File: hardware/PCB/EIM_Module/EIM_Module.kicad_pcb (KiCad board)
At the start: 4 copper layers, 164 parts, among them J1 ADC, J2 CURRENT_PUMP_2, J3 VOLTAGE_MEASUREMENT_1, J4 VOLTAGE_MEASUREMENT_2, J5 PROG, J7 Digital PSU, J8 CURRENT_PUMP_1, J9 Analog PSU, U1 AD9834BRUZ, U10 AD8066ARZ-R7, U2 AD8130ARZ, U3 AD8014ARZ, U4 AD8130ARZ, U5 AD8066ARZ-R7, U6 AD8130ARZ, U7 AD8066ARZ-R7, U8 AD8130ARZ, U9 AD8302ARUZ, Y2 75MHz

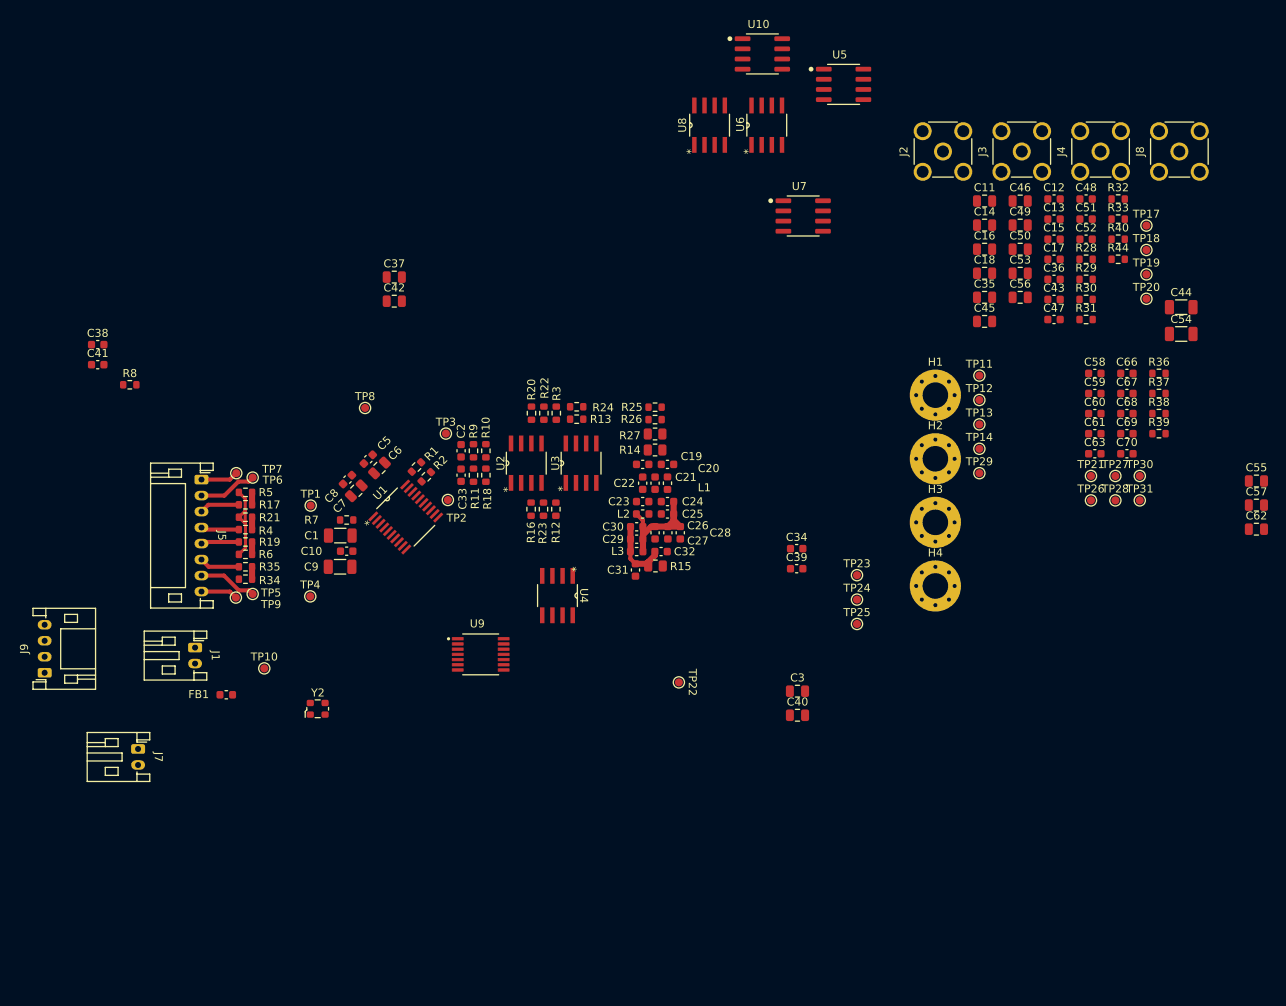
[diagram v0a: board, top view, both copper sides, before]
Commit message: MAMS-38 updated PCB layout for EIM with version using connector
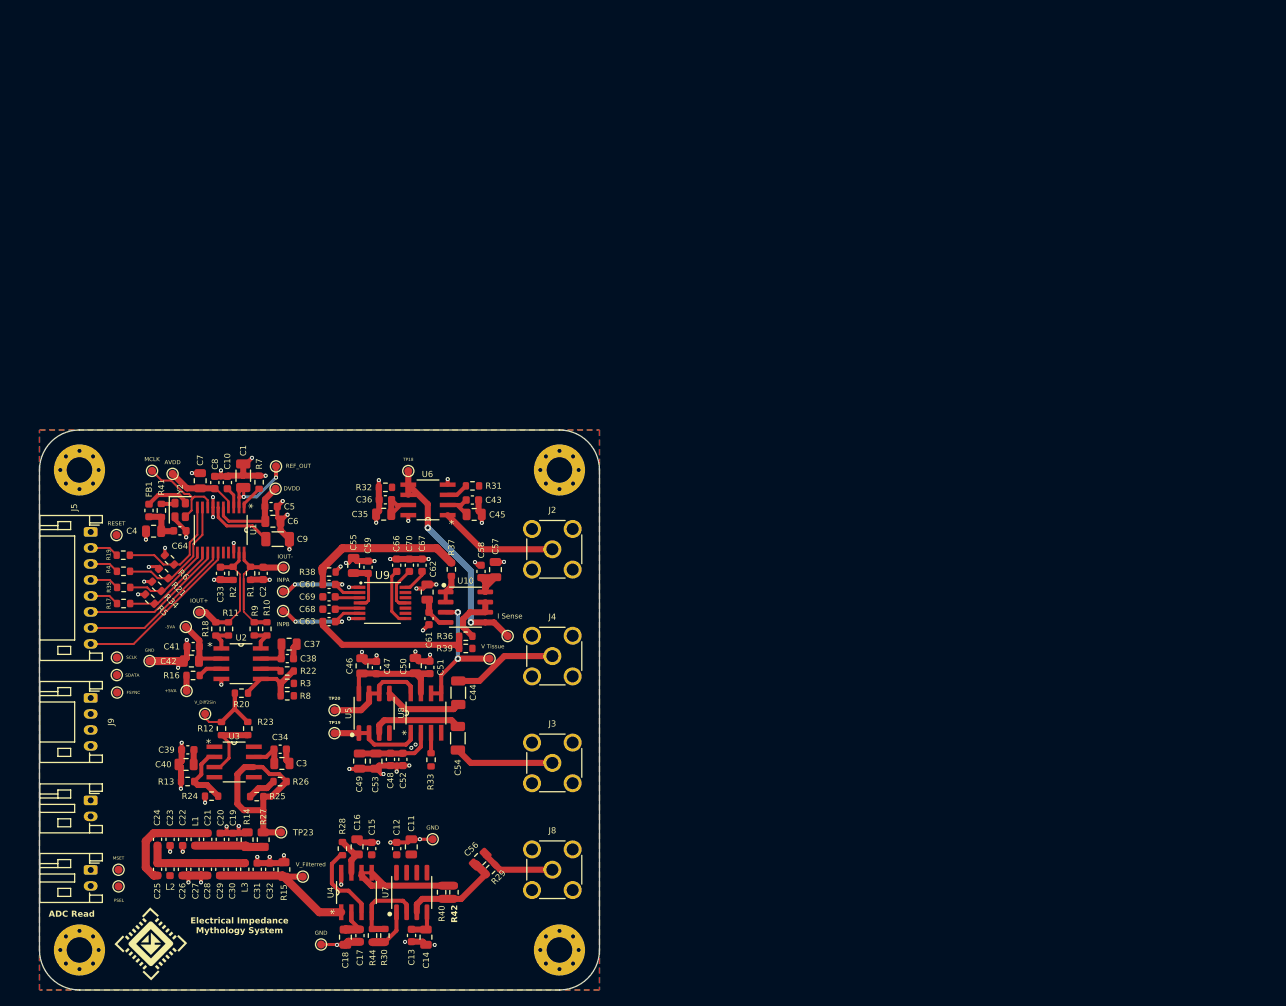
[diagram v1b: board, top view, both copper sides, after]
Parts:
- removed TP1: TP_REFOUT, TestPoint:TestPoint_Pad_D1.0mm
- removed TP10: TP_DIF_SIN, TestPoint:TestPoint_Pad_D1.0mm
- removed TP11: 3.3D, TestPoint:TestPoint_Pad_D1.0mm
- removed TP12: 5VA, TestPoint:TestPoint_Pad_D1.0mm
- removed TP13: -5VA, TestPoint:TestPoint_Pad_D1.0mm
- removed TP14, TP25: GND, TestPoint:TestPoint_Pad_D1.0mm
- removed TP17, TP26: VOUT_BUFFER, TestPoint:TestPoint_Pad_D1.0mm
- removed TP2: TP_IOUT, TestPoint:TestPoint_Pad_D1.0mm
- removed TP21, TP22: VOUT_FILTERED, TestPoint:TestPoint_Pad_D1.0mm
- removed TP24, TP27: VIN_DiffToSingle, TestPoint:TestPoint_Pad_D1.0mm
- removed TP28, TP30, TP31, TP9: TP_GND, TestPoint:TestPoint_Pad_D1.0mm
- removed TP29: 3.3AV, TestPoint:TestPoint_Pad_D1.0mm
- removed TP3: TP_IOUTB, TestPoint:TestPoint_Pad_D1.0mm
- removed TP4: TP_RESET, TestPoint:TestPoint_Pad_D1.0mm
- removed TP5: TP_SDATA, TestPoint:TestPoint_Pad_D1.0mm
- removed TP6: TP_SCLK, TestPoint:TestPoint_Pad_D1.0mm
- removed TP7: TP_FSYNC, TestPoint:TestPoint_Pad_D1.0mm
- removed TP8: TP_MCLK, TestPoint:TestPoint_Pad_D1.0mm
- added +5VA: 5VA, TestPoint:TestPoint_Pad_D1.0mm, F.Cu at (118.4, 102.6)
- added -5VA: -5VA, TestPoint:TestPoint_Pad_D1.0mm, F.Cu at (118.3, 94.6)
- added AVDD: 3.3AV, TestPoint:TestPoint_Pad_D1.0mm, F.Cu at (116.6, 75.5)
- added C4: 10u, Capacitor_SMD:C_0805_2012Metric, F.Cu at (114.3, 82.7)
- added C64: 0.1u, Capacitor_SMD:C_0603_1608Metric, F.Cu at (117.6, 82.6)
- added DVDD: 3.3D, TestPoint:TestPoint_Pad_D1.0mm, F.Cu at (129.5, 77.3)
- added FSYNC: TP_FSYNC, TestPoint:TestPoint_Pad_D1.0mm, F.Cu at (109.7, 102.8)
- added G***: LOGO, dpee_logo_kicad:dpee-logo_10x10, F.Cu at (114.0, 134.2)
- added G***: LOGO, dpee_logo_kicad:DPEE_Footprint, B.Cu at (124.6, 100.7)
- added GND: GND, TestPoint:TestPoint_Pad_D1.0mm, F.Cu at (149.1, 121.2)
- added GND: GND, TestPoint:TestPoint_Pad_D1.0mm, F.Cu at (113.8, 98.9)
- added GND: TP_GND, TestPoint:TestPoint_Pad_D1.0mm, F.Cu at (135.2, 134.3)
- added I Sense: VIN_DiffToSingle, TestPoint:TestPoint_Pad_D1.0mm, F.Cu at (158.5, 95.8)
- added INPA: VOUT_FILTERED, TestPoint:TestPoint_Pad_D1.0mm, F.Cu at (130.5, 90.2)
- added INPB: TP_GND, TestPoint:TestPoint_Pad_D1.0mm, F.Cu at (130.5, 92.6)
- added IOUT+: TP_IOUT, TestPoint:TestPoint_Pad_D1.0mm, F.Cu at (120.0, 92.8)
- added IOUT-: TP_IOUTB, TestPoint:TestPoint_Pad_D1.0mm, F.Cu at (130.5, 87.2)
- added MCLK: TP_MCLK, TestPoint:TestPoint_Pad_D1.0mm, F.Cu at (114.1, 75.1)
- added MSET: TP_GND, TestPoint:TestPoint_Pad_D1.0mm, F.Cu at (109.9, 125.0)
- added PSEL: TP_GND, TestPoint:TestPoint_Pad_D1.0mm, F.Cu at (109.9, 127.1)
- added R41: 10K, Resistor_SMD:R_0603_1608Metric, F.Cu at (115.2, 80.1)
- added R42: 10k, Resistor_SMD:R_0603_1608Metric, F.Cu at (151.8, 127.8)
- added REF_OUT: TP_REFOUT, TestPoint:TestPoint_Pad_D1.0mm, F.Cu at (129.6, 74.5)
- added RESET: TP_RESET, TestPoint:TestPoint_Pad_D1.0mm, F.Cu at (109.6, 83.1)
- added SCLK: TP_SCLK, TestPoint:TestPoint_Pad_D1.0mm, F.Cu at (109.7, 98.5)
- added SDATA: TP_SDATA, TestPoint:TestPoint_Pad_D1.0mm, F.Cu at (109.7, 100.6)
- added V Tissue: VOUT_BUFFER, TestPoint:TestPoint_Pad_D1.0mm, F.Cu at (156.3, 98.6)
- added V_Diff2Sin: TP_DIF_SIN, TestPoint:TestPoint_Pad_D1.0mm, F.Cu at (120.7, 105.5)
- added V_Filterred: VOUT_FILTERED, TestPoint:TestPoint_Pad_D1.0mm, F.Cu at (132.9, 125.8)
- Y2: footprint Oscillator:Oscillator_SMD_ECS_2520MV-xxx-xx-4Pin_2.5x2.0mm -> Oscillator:Oscillator_SMD_SeikoEpson_SG210-4Pin_2.5x2.0mm
- moved R44 125.8 mm to (141.6, 133.2), turned to -90 degrees
- moved C17 121.1 mm to (140.1, 133.2), turned to 90 degrees
- moved C13 120.3 mm to (146.5, 133.2), turned to 90 degrees
- moved H3 119.6 mm to (105.0, 135.0)
- moved J8 119.2 mm to (164.1, 125.0), turned to -90 degrees
- moved R28 118.6 mm to (137.9, 122.3), turned to -90 degrees
- moved R30 118.3 mm to (143.2, 133.2), turned to -90 degrees
- moved R40 117.5 mm to (150.3, 127.8), turned to -90 degrees
- moved TP19 116.6 mm to (136.9, 107.9)
- moved C12 115.5 mm to (144.7, 122.3), turned to -90 degrees
- moved C18 115.2 mm to (138.2, 133.4), turned to 90 degrees
- moved C15 114.4 mm to (141.5, 122.3), turned to -90 degrees
- moved TP20 113.8 mm to (136.9, 105.0)
- moved C55 113.3 mm to (139.3, 86.9), turned to -90 degrees
- moved C14 113.1 mm to (148.3, 133.4), turned to 90 degrees
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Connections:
- net /Voltage Controlled Current Source & Load/+IN_LOAD renamed /Voltage Controlled Current Source & Load/IN_LOAD+
- net /Voltage Controlled Current Source & Load/-IN_LOAD renamed /Voltage Controlled Current Source & Load/IN_LOAD-
- C1 pad 2: AGND -> GND
- C10 pad 1: AGND -> GND
- C11 pad 1: AGND -> GND
- C12 pad 1: AGND -> GND
- C13 pad 1: AGND -> GND
- C14 pad 1: AGND -> GND
- C15 pad 1: AGND -> GND
- C16 pad 1: AGND -> GND
- C17 pad 1: AGND -> GND
- C18 pad 1: AGND -> GND
- C19 pad 1: AGND -> GND
- C2 pad 1: AGND -> GND
- C20 pad 1: AGND -> GND
- C22 pad 1: AGND -> GND
- C23 pad 1: AGND -> GND
- C26 pad 1: AGND -> GND
- C27 pad 1: AGND -> GND
- C28 pad 1: AGND -> GND
- C3 pad 1: AGND -> GND
- C31 pad 1: AGND -> GND
- C32 pad 1: AGND -> GND
- C33 pad 1: AGND -> GND
- C34 pad 1: AGND -> GND
- C35 pad 1: AGND -> GND
- C36 pad 1: AGND -> GND
- C37 pad 1: AGND -> GND
- C38 pad 1: AGND -> GND
- C39 pad 1: AGND -> GND
- C40 pad 1: AGND -> GND
- C41 pad 1: AGND -> GND
- C42 pad 1: AGND -> GND
- C43 pad 1: AGND -> GND
- C45 pad 1: AGND -> GND
- C46 pad 1: AGND -> GND
- C47 pad 1: AGND -> GND
- C48 pad 1: AGND -> GND
- C49 pad 1: AGND -> GND
- C5 pad 1: AGND -> GND
- C50 pad 1: AGND -> GND
- C51 pad 1: AGND -> GND
- C52 pad 1: AGND -> GND
- C53 pad 1: AGND -> GND
- C55 pad 1: AGND -> GND
- C57 pad 1: AGND -> GND
- C58 pad 1: AGND -> GND
- C59 pad 1: AGND -> GND
- C6 pad 1: AGND -> GND
- C61 pad 1: AGND -> GND
- C62 pad 1: AGND -> GND
- C66 pad 2: AGND -> GND
- C67 pad 2: AGND -> GND
- C68 pad 1: AGND -> GND
- C69 pad 1: AGND -> GND
- C7 pad 1: AGND -> GND
- C70 pad 1: AGND -> GND
- C8 pad 1: AGND -> GND
- C9 pad 1: AGND -> GND
- H1 pad 1: AGND -> GND
- H2 pad 1: AGND -> GND
- H3 pad 1: AGND -> GND
- H4 pad 1: AGND -> GND
- J2 pad 2: AGND -> GND
- J3 pad 2: AGND -> GND
- J4 pad 2: AGND -> GND
- J5 pad 1: /Signal Generator & Differential to Single/FSYNC -> GND
- J5 pad 2: /Signal Generator & Differential to Single/SCLK -> /Signal Generator & Differential to Single/PSELECT_uC
- J5 pad 3: /Signal Generator & Differential to Single/PIN_3 -> /Signal Generator & Differential to Single/FSELECT_uC
- J5 pad 4: Net-(J5-Pin_4) -> /Signal Generator & Differential to Single/RESET_uC
- J5 pad 5: /Signal Generator & Differential to Single/PIN_5 -> /Signal Generator & Differential to Single/SLEEP_uC
- J5 pad 6: /Signal Generator & Differential to Single/PIN_6 -> /Signal Generator & Differential to Single/SDATA
- J5 pad 7: /Signal Generator & Differential to Single/SDATA -> /Signal Generator & Differential to Single/SCLK
- J5 pad 8: AGND -> /Signal Generator & Differential to Single/FSYNC
- J7 pad 1: AGND -> GND
- J8 pad 2: AGND -> GND
- J9 pad 1: AGND -> GND
- R1 pad 1: AGND -> GND
- R13 pad 1: AGND -> GND
- R14 pad 1: AGND -> GND
- R15 pad 1: AGND -> GND
- R17 pad 1: /Signal Generator & Differential to Single/PIN_3 -> /Signal Generator & Differential to Single/SLEEP_uC
- R19 pad 1: /Signal Generator & Differential to Single/PIN_5 -> /Signal Generator & Differential to Single/PSELECT_uC
- R2 pad 1: AGND -> GND
- R21 pad 1: AGND -> GND
- R24 pad 1: AGND -> GND
- R3 pad 1: AGND -> GND
- R32 pad 2: AGND -> GND
- R34 pad 1: AGND -> GND
- R35 pad 1: /Signal Generator & Differential to Single/PIN_6 -> /Signal Generator & Differential to Single/RESET_uC
- R38 pad 1: AGND -> GND
- R39 pad 1: AGND -> GND
- R4 pad 1: Net-(J5-Pin_4) -> /Signal Generator & Differential to Single/FSELECT_uC
- R5 pad 1: AGND -> GND
- R6 pad 1: AGND -> GND
- R7 pad 1: AGND -> GND
- R8 pad 1: AGND -> GND
- U1 pad 18: AGND -> GND
- U1 pad 7: AGND -> GND
- U2 pad 4: AGND -> GND
- U4 pad 8: AGND -> GND
- U6 pad 4: AGND -> GND
- U6 pad 8: AGND -> GND
- U7 pad 5: AGND -> GND
- U8 pad 4: AGND -> GND
- U9 pad 1: AGND -> GND
- U9 pad 7: AGND -> GND
- Y2 pad 1: unconnected-(Y2-Tri-State-Pad1) -> Net-(Y2-Tri-State)
- Y2 pad 2: AGND -> GND
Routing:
- net GND: track 0.00 -> 135.7 mm, vias 0 -> 67
- net +5V: track 0.00 -> 51.3 mm
- net -5V: track 0.00 -> 37.7 mm
- net /Gain & Phase detector/I_SENSE_RAW: track 0.00 -> 28.7 mm, vias 0 -> 2
- net /Buffer & Filter blocks/VOUT_BUFFER: track 0.00 -> 25.0 mm
- net /Gain & Phase detector/to_INPB: track 0.00 -> 20.2 mm
- net /Gain & Phase detector/to_INPA: track 0.00 -> 20.0 mm
- net /Signal Generator & Differential to Single/IOUT+: track 0.00 -> 19.7 mm
- net /Signal Generator & Differential to Single/IOUT-: track 0.00 -> 19.6 mm
- net /Gain & Phase detector/V_TISSUE_RAW: track 0.00 -> 17.8 mm, vias 0 -> 2
- net /Voltage Controlled Current Source & Load/FB_VCCS: track 0.00 -> 17.5 mm
- net /Signal Generator & Differential to Single/FSYNC: track 4.68 -> 21.2 mm
- net +3.3V: track 0.00 -> 16.1 mm
- net AGND: track 15.3 -> 0.00 mm
- net /Voltage Controlled Current Source & Load/CURRENT_PUMP_2: track 0.00 -> 14.8 mm
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- added copper zone on B.Cu, net GND
- added copper zone on F.Cu, net GND
- added copper zone on In1.Cu, net GND
- added copper zone on In2.Cu, net GND
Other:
- board outline added: 70 x 70 mm
- board text added: "ADC Read"
- board text added: "Electrical Impedance Mythology System"

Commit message: MAMS-40 Updated PCB upto LPF
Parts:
- removed +5VA: 5VA, TestPoint:TestPoint_Pad_D1.0mm
- removed -5VA: -5VA, TestPoint:TestPoint_Pad_D1.0mm
- removed AVDD: 3.3AV, TestPoint:TestPoint_Pad_D1.0mm
- removed C70: 0.1u, Capacitor_SMD:C_0603_1608Metric
- removed DVDD: 3.3D, TestPoint:TestPoint_Pad_D1.0mm
- removed FSYNC: TP_FSYNC, TestPoint:TestPoint_Pad_D1.0mm
- removed the G*** at (114.0, 134.2)
- removed GND (x2): GND, TestPoint:TestPoint_Pad_D1.0mm
- removed GND, INPB, MSET, PSEL: TP_GND, TestPoint:TestPoint_Pad_D1.0mm
- removed I Sense: VIN_DiffToSingle, TestPoint:TestPoint_Pad_D1.0mm
- removed INPA, V_Filterred: VOUT_FILTERED, TestPoint:TestPoint_Pad_D1.0mm
- removed IOUT+: TP_IOUT, TestPoint:TestPoint_Pad_D1.0mm
- removed IOUT-: TP_IOUTB, TestPoint:TestPoint_Pad_D1.0mm
- removed J1: ADC, Connector_JST:JST_PH_S2B-PH-K_1x02_P2.00mm_Horizontal
- removed J7: Digital PSU, Connector_JST:JST_PH_S2B-PH-K_1x02_P2.00mm_Horizontal
- removed J9: Analog PSU, Connector_JST:JST_PH_S4B-PH-K_1x04_P2.00mm_Horizontal
- removed MCLK: TP_MCLK, TestPoint:TestPoint_Pad_D1.0mm
- removed REF_OUT: TP_REFOUT, TestPoint:TestPoint_Pad_D1.0mm
- removed RESET: TP_RESET, TestPoint:TestPoint_Pad_D1.0mm
- removed SCLK: TP_SCLK, TestPoint:TestPoint_Pad_D1.0mm
- removed SDATA: TP_SDATA, TestPoint:TestPoint_Pad_D1.0mm
- removed V Tissue: VOUT_BUFFER, TestPoint:TestPoint_Pad_D1.0mm
- removed V_Diff2Sin: TP_DIF_SIN, TestPoint:TestPoint_Pad_D1.0mm
- added G***: LOGO, dpee_logo_kicad:dpee-logo_6x6, F.Cu at (144.0, 87.5)
- added TP1: TP_REFOUT, TestPoint:TestPoint_Pad_D1.0mm, F.Cu at (358.2, -9.72)
- added TP10: TP_DIF_SIN, TestPoint:TestPoint_Pad_D1.0mm, F.Cu at (361.2, 2.48)
- added TP11: 3.3D, TestPoint:TestPoint_Pad_D1.0mm, F.Cu at (368.5, 34.8)
- added TP12: 5VA, TestPoint:TestPoint_Pad_D1.0mm, F.Cu at (368.5, 37.9)
- added TP13: -5VA, TestPoint:TestPoint_Pad_D1.0mm, F.Cu at (368.5, 40.9)
- added TP14: GND, TestPoint:TestPoint_Pad_D1.0mm, F.Cu at (368.5, 44.0)
- added TP17: VOUT_BUFFER, TestPoint:TestPoint_Pad_D1.0mm, F.Cu at (353.1, 12.5)
- added TP2: TP_IOUT, TestPoint:TestPoint_Pad_D1.0mm, F.Cu at (358.2, -6.67)
- added TP21: VOUT_FILTERED, TestPoint:TestPoint_Pad_D1.0mm, F.Cu at (338.3, 34.8)
- added TP22: VOUT_FILTERED, TestPoint:TestPoint_Pad_D1.0mm, F.Cu at (331.8, 34.8)
- added TP25: GND, TestPoint:TestPoint_Pad_D1.0mm, F.Cu at (331.8, 40.9)
- added TP27: VIN_DiffToSingle, TestPoint:TestPoint_Pad_D1.0mm, F.Cu at (338.3, 37.9)
- added TP28: TP_GND, TestPoint:TestPoint_Pad_D1.0mm, F.Cu at (338.3, 40.9)
- added TP29: 3.3AV, TestPoint:TestPoint_Pad_D1.0mm, F.Cu at (368.5, 47.0)
- added TP3: TP_IOUTB, TestPoint:TestPoint_Pad_D1.0mm, F.Cu at (358.2, -3.62)
- added TP30: TP_GND, TestPoint:TestPoint_Pad_D1.0mm, F.Cu at (338.3, 44.0)
- added TP31: TP_GND, TestPoint:TestPoint_Pad_D1.0mm, F.Cu at (338.3, 47.0)
- added TP4: TP_RESET, TestPoint:TestPoint_Pad_D1.0mm, F.Cu at (358.2, -0.57)
- added TP5: TP_SDATA, TestPoint:TestPoint_Pad_D1.0mm, F.Cu at (358.2, 2.48)
- added TP6: TP_SCLK, TestPoint:TestPoint_Pad_D1.0mm, F.Cu at (361.2, -9.72)
- added TP7: TP_FSYNC, TestPoint:TestPoint_Pad_D1.0mm, F.Cu at (361.2, -6.67)
- added TP8: TP_MCLK, TestPoint:TestPoint_Pad_D1.0mm, F.Cu at (361.2, -3.62)
- added TP9: TP_GND, TestPoint:TestPoint_Pad_D1.0mm, F.Cu at (361.2, -0.57)
- C3: value 10u -> 20p; footprint Capacitor_SMD:C_0805_2012Metric -> Capacitor_SMD:C_0603_1608Metric
- C33: value 20p -> 10u; footprint Capacitor_SMD:C_0603_1608Metric -> Capacitor_SMD:C_0805_2012Metric
- J5: value PROG -> Interface with controller; footprint Connector_JST:JST_PH_S8B-PH-K_1x08_P2.00mm_Horizontal -> Connector_PinHeader_2.00mm:PinHeader_2x14_P2.00mm_Vertical; moved to B.Cu
- moved TP19 233.9 mm to (353.1, 18.6)
- moved TP20 231.7 mm to (353.1, 21.6)
- moved TP23 217.8 mm to (331.8, 37.9)
- moved TP18 215.4 mm to (353.1, 15.5)
- moved H3 98.5 mm to (145.0, 45.0)
- moved H1 94.9 mm to (195.0, 45.0)
- moved C3 61.5 mm to (159.4, 57.5), turned to 90 degrees
- moved C4 60.7 mm to (165.6, 50.4), turned to 180 degrees
- moved C68 59.7 mm to (184.5, 57.4)
- moved C49 59.2 mm to (184.6, 72.4), turned to 0 degrees
- moved C64 58.7 mm to (165.4, 48.6)
- moved C69 57.4 mm to (184.5, 59.9)
- moved C55 57.2 mm to (184.5, 51.8), turned to 0 degrees
- moved C35 56.3 mm to (185.0, 43.0)
- moved R38 54.5 mm to (184.5, 62.4), turned to 0 degrees
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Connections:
- C11 pad 2: +5V -> +5VA
- C12 pad 2: +5V -> +5VA
- C13 pad 2: -5V -> -5VA
- C14 pad 2: -5V -> -5VA
- C15 pad 2: +5V -> +5VA
- C16 pad 2: +5V -> +5VA
- C17 pad 2: -5V -> -5VA
- C18 pad 2: -5V -> -5VA
- C3 pad 2: +5V -> /Signal Generator & Differential to Single/IOUT+
- C33 pad 2: /Signal Generator & Differential to Single/IOUT+ -> +5VA
- C34 pad 2: +5V -> +5VA
- C35 pad 2: +5V -> +5VA
- C36 pad 2: +5V -> +5VA
- C37 pad 2: +5V -> +5VA
- C38 pad 2: +5V -> +5VA
- C39 pad 2: -5V -> -5VA
- C40 pad 2: -5V -> -5VA
- C41 pad 2: -5V -> -5VA
- C42 pad 2: -5V -> -5VA
- C43 pad 2: -5V -> -5VA
- C45 pad 2: -5V -> -5VA
- C46 pad 2: +5V -> +5VA
- C47 pad 2: +5V -> +5VA
- C48 pad 2: -5V -> -5VA
- C49 pad 2: -5V -> -5VA
- C50 pad 2: +5V -> +5VA
- C51 pad 2: +5V -> +5VA
- C52 pad 2: -5V -> -5VA
- C53 pad 2: -5V -> -5VA
- C55 pad 2: +5V -> +5VA
- C57 pad 2: +5V -> +5VA
- C58 pad 2: +5V -> +5VA
- C59 pad 2: +5V -> +5VA
- C61 pad 2: -5V -> -5VA
- C62 pad 2: -5V -> -5VA
- J5 pad 2: /Signal Generator & Differential to Single/PSELECT_uC -> /Signal Generator & Differential to Single/SDATA
- J5 pad 3: /Signal Generator & Differential to Single/FSELECT_uC -> +3.3V
- J5 pad 4: /Signal Generator & Differential to Single/RESET_uC -> GND
- J5 pad 5: /Signal Generator & Differential to Single/SLEEP_uC -> GND
- J5 pad 6: /Signal Generator & Differential to Single/SDATA -> /Signal Generator & Differential to Single/SCLK
- J5 pad 7: /Signal Generator & Differential to Single/SCLK -> /Signal Generator & Differential to Single/PSELECT_uC
- J5 pad 8: /Signal Generator & Differential to Single/FSYNC -> GND
- R16 pad 1: +5V -> +5VA
- R28 pad 1: +5V -> +5VA
- R31 pad 1: +5V -> +5VA
- R33 pad 1: +5V -> +5VA
- R34 pad 1: GND -> +3.3V
- U10 pad 4: -5V -> -5VA
- U10 pad 8: +5V -> +5VA
- U2 pad 2: -5V -> -5VA
- U2 pad 7: +5V -> +5VA
- U3 pad 4: -5V -> -5VA
- U3 pad 7: +5V -> +5VA
- U4 pad 2: -5V -> -5VA
- U4 pad 7: +5V -> +5VA
- U5 pad 4: -5V -> -5VA
- U5 pad 8: +5V -> +5VA
- U6 pad 2: -5V -> -5VA
- U6 pad 7: +5V -> +5VA
- U7 pad 4: -5V -> -5VA
- U7 pad 8: +5V -> +5VA
- U8 pad 2: -5V -> -5VA
- U8 pad 7: +5V -> +5VA
- U9 pad 11: /Gain & Phase detector/VREF -> unconnected-(U9-VREF-Pad11)
- U9 pad 4: +5V -> +5VA
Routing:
- net GND: track 135.7 -> 27.9 mm, vias 67 -> 26
- net +5V: track 51.3 -> 0.00 mm
- net -5V: track 37.7 -> 0.00 mm
- net /Gain & Phase detector/I_SENSE_RAW: track 28.7 -> 0.00 mm, vias 2 -> 0
- net /Gain & Phase detector/to_INPB: track 20.2 -> 0.00 mm
- net /Gain & Phase detector/to_INPA: track 20.0 -> 0.00 mm
- net /Gain & Phase detector/V_TISSUE_RAW: track 17.8 -> 0.00 mm, vias 2 -> 0
- net /Voltage Controlled Current Source & Load/FB_VCCS: track 17.5 -> 0.00 mm
- net /Buffer & Filter blocks/VOUT_BUFFER: track 25.0 -> 9.36 mm
- net /Voltage Controlled Current Source & Load/CURRENT_PUMP_2: track 14.8 -> 0.00 mm
- net /Voltage Controlled Current Source & Load/IN_LOAD-: track 13.3 -> 0.00 mm
- net /Voltage Controlled Current Source & Load/+IN_A_VCCS: track 13.1 -> 0.00 mm
- net /Voltage Controlled Current Source & Load/-IN_B_LOAD: track 13.0 -> 0.00 mm
- net /Voltage Controlled Current Source & Load/+IN_A_LOAD: track 12.5 -> 0.00 mm
- net /Gain & Phase detector/INPB: track 12.2 -> 0.00 mm, vias 2 -> 0
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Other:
- board size 70 x 70 mm -> 60 x 60 mm
- board text removed: "ADC Read"
- board text removed: "Electrical Impedance Mythology System"
